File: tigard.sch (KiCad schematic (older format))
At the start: 84 parts, among them J1 USB_C_Receptacle_USB2.0, J2 JTAG, J3 UART, J4 SPI, J5 SWD, J6 I2C, Q1 BSH103, SW1 SW_DP4T, SW2 SW_DPDT, U1 AP7365-18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

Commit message: Layout routing complete, RHL fixes, xtal caps
* Finish first round of routing (needs to be reviewed, reworked in some
  places probably)
* Fix the RHL footprint (paste shouldn't be copper layers, thermal pad
  should be a polygon)
* Add 30pF capacitors to the xtal (based off estimated Cstray of 5pF)
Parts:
- added C23, C24: 30pF, Capacitor_SMD:C_0402_1005Metric, symbol Device:C_Small
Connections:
- net GND: now also C23.2, C24.2
- net USB_DN: now also J1.A7 (D-), J1.B7 (D-)
- net USB_DP: now also J1.A6 (D+), J1.B6 (D+)
- net at U3.2 (OSCI), Y1.1: now also C23.1
- net at U3.3 (OSCO), Y1.3: now also C24.1
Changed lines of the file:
@@
 NoConn ~ 1900 2100
 NoConn ~ 1900 2200
-Text Label 2600 1700 2    50   ~ 0
+Text Label 2250 1800 2    50   ~ 0
 USB_DP
-Text Label 2600 1600 2    50   ~ 0
+Text Label 2250 1600 2    50   ~ 0
 USB_DN
 $Comp
@@
 U 1 1 5EE8326F
 P 1100 7850
-F 0 "Y1" V 1054 7607 50  0000 R CNN
-F 1 "12MHz" V 1145 7607 50  0000 R CNN
+F 0 "Y1" V 1050 7550 50  0000 L CNN
+F 1 "12MHz" V 1150 7450 50  0000 L CNN
 F 2 "Crystal:Crystal_SMD_3225-4Pin_3.2x2.5mm" H 1100 7850 50  0001 C CNN
 F 3 "~" H 1100 7850 50  0001 C CNN
@@
 $EndComp
 Wire Wire Line
-	900  7850 900  8250
-Wire Wire Line
-	900  8250 1400 8250
-Wire Wire Line
 	1400 8300 1400 8250
-Connection ~ 1400 8250
-Wire Wire Line
-	1400 8250 1500 8250
 $Comp
 L power:GND #PWR0129
@@
 	1    0    0    -1
 $EndComp
+$Comp
+L Device:C_Small C23
+U 1 1 5EE9988B
+P 850 7650
+F 0 "C23" V 621 7650 50  0000 C CNN
+F 1 "30pF" V 712 7650 50  0000 C CNN
+F 2 "Capacitor_SMD:C_0402_1005Metric" H 850 7650 50  0001 C CNN
+F 3 "~" H 850 7650 50  0001 C CNN
+F 4 "CL05C300JB5NNNC" V 850 7650 50  0001 C CNN "P/N"
+F 5 "C159804" V 850 7650 50  0001 C CNN "LCSC"
+F 6 "cap-cer-0402-22pF" V 850 7650 50  0001 C CNN "Key"
+	1    850  7650
+	0    1    1    0
+$EndComp
+Wire Wire Line
+	1400 8250 1500 8250
+Wire Wire Line
+	950  7650 1100 7650
+Connection ~ 1100 7650
+Wire Wire Line
+	950  8050 1100 8050
+Connection ~ 1100 8050
+$Comp
+L power:GND #PWR01
+U 1 1 5F06B15D
+P 650 8050
+F 0 "#PWR01" H 650 7800 50  0001 C CNN
+F 1 "GND" H 655 7877 50  0000 C CNN
+F 2 "" H 650 8050 50  0001 C CNN
+F 3 "" H 650 8050 50  0001 C CNN
+	1    650  8050
+	1    0    0    -1
+$EndComp
+Wire Wire Line
+	650  8050 750  8050
+Wire Wire Line
+	900  7850 650  7850
+Wire Wire Line
+	650  7850 650  8050
+Connection ~ 650  8050
+Wire Wire Line
+	750  7650 650  7650
+Wire Wire Line
+	650  7650 650  7850
+Connection ~ 650  7850
+$Comp
+L Device:C_Small C24
+U 1 1 5F135A55
+P 850 8050
+F 0 "C24" V 987 8050 50  0000 C CNN
+F 1 "30pF" V 1078 8050 50  0000 C CNN
+F 2 "Capacitor_SMD:C_0402_1005Metric" H 850 8050 50  0001 C CNN
+F 3 "~" H 850 8050 50  0001 C CNN
+F 4 "CL05C300JB5NNNC" V 850 8050 50  0001 C CNN "P/N"
+F 5 "C159804" V 850 8050 50  0001 C CNN "LCSC"
+F 6 "cap-cer-0402-22pF" V 850 8050 50  0001 C CNN "Key"
+	1    850  8050
+	0    1    1    0
+$EndComp
+Wire Wire Line
+	1900 1800 1950 1800
+Wire Wire Line
+	2250 1600 1950 1600
+Wire Wire Line
+	1900 1700 1950 1700
+Wire Wire Line
+	1950 1700 1950 1800
+Connection ~ 1950 1800
+Wire Wire Line
+	1950 1800 2250 1800
+Wire Wire Line
+	1900 1500 1950 1500
+Wire Wire Line
+	1950 1500 1950 1600
+Connection ~ 1950 1600
+Wire Wire Line
+	1950 1600 1900 1600
 $EndSCHEMATC

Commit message: Redesign
* Designed completely in metric, no mixing units
* RoundRect pads
* Comb for resistor arrays
* VREG on inner power layer
* Switch to SMD SWD connector
* OSHW logo on front & back
* License and copyright info
* Remove reference designators
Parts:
- J5: footprint Connector_PinHeader_1.27mm:PinHeader_2x05_P1.27mm_Vertical -> Connector_PinHeader_1.27mm:PinHeader_2x05_P1.27mm_Vertical_SMD
- Q1: footprint Package_TO_SOT_SMD:SOT-23 -> tigard:SOT-23_RoundRect
- RN1, RN2, RN3, RN4, RN5, RN6, RN7, RN8: footprint Resistor_SMD:R_Array_Convex_4x0402 -> tigard:R_Array_Convex_4x0402_RoundRect
- U1, U2: footprint Package_TO_SOT_SMD:SOT-23-5 -> tigard:SOT-23-5_RoundRect
- U4: footprint Package_TO_SOT_SMD:SOT-23-6 -> tigard:SOT-23-6_RoundRect
- Y1: footprint Crystal:Crystal_SMD_3225-4Pin_3.2x2.5mm -> tigard:Crystal_SMD_3225-4Pin_3.2x2.5mm_RoundRect
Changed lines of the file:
@@
 NoConn ~ 1900 2100
 NoConn ~ 1900 2200
-Text Label 2250 1800 2    50   ~ 0
-USB_DP
-Text Label 2250 1600 2    50   ~ 0
-USB_DN
 $Comp
 L Device:R_Small R1
@@
 F 0 "U1" H 3600 1375 50  0000 C CNN
 F 1 "AP7365-18" H 3600 1284 50  0000 C CNN
-F 2 "Package_TO_SOT_SMD:SOT-23-5" H 3700 1350 50  0001 C CNN
+F 2 "tigard:SOT-23-5_RoundRect" H 3700 1350 50  0001 C CNN
 F 3 "" H 3600 1050 50  0001 C CNN
 F 4 "AP7365-18WG-7" H 3600 1450 50  0001 C CNN "P/N"
@@
 F 0 "U2" H 5100 1375 50  0000 C CNN
 F 1 "AP7365-33" H 5100 1284 50  0000 C CNN
-F 2 "Package_TO_SOT_SMD:SOT-23-5" H 5200 1350 50  0001 C CNN
+F 2 "tigard:SOT-23-5_RoundRect" H 5200 1350 50  0001 C CNN
 F 3 "" H 5100 1050 50  0001 C CNN
 F 4 "AP7365-33WG-7" H 5100 1450 50  0001 C CNN "P/N"
@@
 F 0 "Q1" H 7655 1946 50  0000 L CNN
 F 1 "BSH103" H 7655 1855 50  0000 L CNN
-F 2 "Package_TO_SOT_SMD:SOT-23" H 7650 2000 50  0001 C CNN
+F 2 "tigard:SOT-23_RoundRect" H 7650 2000 50  0001 C CNN
 F 3 "~" H 7450 1900 50  0001 C CNN
 F 4 "BSH103,235" H 7450 1900 50  0001 C CNN "P/N"
@@
 F 0 "J5" H 10400 2817 50  0000 C CNN
 F 1 "SWD" H 10400 2726 50  0000 C CNN
-F 2 "Connector_PinHeader_1.27mm:PinHeader_2x05_P1.27mm_Vertical" H 10350 2400 50  0001 C CNN
+F 2 "Connector_PinHeader_1.27mm:PinHeader_2x05_P1.27mm_Vertical_SMD" H 10350 2400 50  0001 C CNN
 F 3 "~" H 10350 2400 50  0001 C CNN
 F 4 "20021111-00010T4LF" H 10350 2400 50  0001 C CNN "P/N"
@@
 $EndComp
 NoConn ~ 10150 2500
-NoConn ~ 10650 2500
-NoConn ~ 10650 2400
 Text Label 9800 2200 0    50   ~ 0
 VTARGET
 Text Label 10900 2200 2    50   ~ 0
 SWDIO
-Text Label 10900 2300 2    50   ~ 0
-TCK
 Text Label 10900 2600 2    50   ~ 0
 ~SRST
 Wire Wire Line
 	10900 2600 10650 2600
-Wire Wire Line
-	10900 2300 10650 2300
 Wire Wire Line
 	10650 2200 10900 2200
@@
 F 0 "Y1" V 1050 7550 50  0000 L CNN
 F 1 "12MHz" V 1150 7450 50  0000 L CNN
-F 2 "Crystal:Crystal_SMD_3225-4Pin_3.2x2.5mm" H 1100 7850 50  0001 C CNN
+F 2 "tigard:Crystal_SMD_3225-4Pin_3.2x2.5mm_RoundRect" H 1100 7850 50  0001 C CNN
 F 3 "~" H 1100 7850 50  0001 C CNN
 F 4 "X322512MSB4SI" V 1100 7850 50  0001 C CNN "P/N"
@@
 F 0 "U4" H 3100 9900 50  0000 C CNN
 F 1 "93LC46BT-I/OT" H 3050 9800 50  0000 C CNN
-F 2 "Package_TO_SOT_SMD:SOT-23-6" H 2700 10100 50  0001 C CNN
+F 2 "tigard:SOT-23-6_RoundRect" H 2700 10100 50  0001 C CNN
 F 3 "http://ww1.microchip.com/downloads/en/DeviceDoc/20001749K.pdf" H 2700 10100 50  0001 C CNN
 F 4 "93LC56BT-I/OT" H 2700 10100 50  0001 C CNN "P/N"
@@
 Wire Wire Line
 	5450 5100 5450 5200
-$Comp
-L Device:R_Pack04 RN1
-U 1 1 5FBD884A
-P 5250 5650
-F 0 "RN1" V 4833 5650 50  0000 C CNN
-F 1 "100k" V 4924 5650 50  0000 C CNN
-F 2 "Resistor_SMD:R_Array_Convex_4x0402" V 5525 5650 50  0001 C CNN
-F 3 "~" H 5250 5650 50  0001 C CNN
-F 4 "4D02WGJ0104TCE" V 5250 5650 50  0001 C CNN "P/N"
-F 5 "C25724" V 5250 5650 50  0001 C CNN "LCSC"
-F 6 "res-0402cv-array-4-100k" V 5250 5650 50  0001 C CNN "Key"
-	1    5250 5650
-	0    1    1    0
-$EndComp
 Wire Wire Line
 	5050 6150 5000 6150
@@
 Wire Wire Line
 	7100 7150 7500 7150
-$Comp
-L Device:R_Pack04 RN5
-U 1 1 601ADA09
-P 5550 7500
-F 0 "RN5" V 5133 7500 50  0000 C CNN
-F 1 "100" V 5224 7500 50  0000 C CNN
-F 2 "Resistor_SMD:R_Array_Convex_4x0402" V 5825 7500 50  0001 C CNN
-F 3 "~" H 5550 7500 50  0001 C CNN
-F 4 "4D02WGJ0101TCE" V 5550 7500 50  0001 C CNN "P/N"
-F 5 "C48442" V 5550 7500 50  0001 C CNN "LCSC"
-F 6 "res-0402cv-array-4-100" V 5550 7500 50  0001 C CNN "Key"
-	1    5550 7500
-	0    1    1    0
-$EndComp
 Wire Wire Line
 	5350 8000 5300 8000
@@
 	7050 4400 7450 4400
 $Comp
-L Device:R_Pack04 RN6
-U 1 1 611E05C2
-P 5550 7900
-F 0 "RN6" V 5783 7900 50  0000 C CNN
-F 1 "100" V 5874 7900 50  0000 C CNN
-F 2 "Resistor_SMD:R_Array_Convex_4x0402" V 5825 7900 50  0001 C CNN
-F 3 "~" H 5550 7900 50  0001 C CNN
-F 4 "4D02WGJ0101TCE" V 5550 7900 50  0001 C CNN "P/N"
-F 5 "C48442" V 5550 7900 50  0001 C CNN "LCSC"
-F 6 "res-0402cv-array-4-100" V 5550 7900 50  0001 C CNN "Key"
-	1    5550 7900
-	0    1    1    0
-$EndComp
-$Comp
 L Device:R_Pack04 RN3
 U 1 1 6123B61B
@@
 F 0 "RN3" V 7033 5650 50  0000 C CNN
 F 1 "100" V 7124 5650 50  0000 C CNN
-F 2 "Resistor_SMD:R_Array_Convex_4x0402" V 7725 5650 50  0001 C CNN
+F 2 "tigard:R_Array_Convex_4x0402_RoundRect" V 7725 5650 50  0001 C CNN
 F 3 "~" H 7450 5650 50  0001 C CNN
 F 4 "4D02WGJ0101TCE" V 7450 5650 50  0001 C CNN "P/N"
@@
 $EndComp
 $Comp
-L Device:R_Pack04 RN4
-U 1 1 6123C1F3
-P 7450 6050
-F 0 "RN4" V 7683 6050 50  0000 C CNN
-F 1 "100" V 7774 6050 50  0000 C CNN
-F 2 "Resistor_SMD:R_Array_Convex_4x0402" V 7725 6050 50  0001 C CNN
-F 3 "~" H 7450 6050 50  0001 C CNN
-F 4 "4D02WGJ0101TCE" V 7450 6050 50  0001 C CNN "P/N"
-F 5 "C48442" V 7450 6050 50  0001 C CNN "LCSC"
-F 6 "res-0402cv-array-4-100" V 7450 6050 50  0001 C CNN "Key"
-	1    7450 6050
-	0    1    1    0
-$EndComp
-$Comp
-L Device:R_Pack04 RN2
-U 1 1 612C4752
-P 5250 6050
-F 0 "RN2" V 5483 6050 50  0000 C CNN
-F 1 "100k" V 5574 6050 50  0000 C CNN
-F 2 "Resistor_SMD:R_Array_Convex_4x0402" V 5525 6050 50  0001 C CNN
-F 3 "~" H 5250 6050 50  0001 C CNN
-F 4 "4D02WGJ0104TCE" V 5250 6050 50  0001 C CNN "P/N"
-F 5 "C25724" V 5250 6050 50  0001 C CNN "LCSC"
-F 6 "res-0402cv-array-4-100k" V 5250 6050 50  0001 C CNN "Key"
-	1    5250 6050
-	0    1    1    0
-$EndComp
-$Comp
 L Device:R_Pack04 RN7
 U 1 1 612C4DF4
@@
 F 0 "RN7" V 7333 7500 50  0000 C CNN
 F 1 "100k" V 7424 7500 50  0000 C CNN
-F 2 "Resistor_SMD:R_Array_Convex_4x0402" V 8025 7500 50  0001 C CNN
+F 2 "tigard:R_Array_Convex_4x0402_RoundRect" V 8025 7500 50  0001 C CNN
 F 3 "~" H 7750 7500 50  0001 C CNN
 F 4 "4D02WGJ0104TCE" V 7750 7500 50  0001 C CNN "P/N"
@@
 F 6 "res-0402cv-array-4-100k" V 7750 7500 50  0001 C CNN "Key"
 	1    7750 7500
-	0    1    1    0
-$EndComp
-$Comp
-L Device:R_Pack04 RN8
-U 1 1 612C5897
-P 7750 7900
-F 0 "RN8" V 7983 7900 50  0000 C CNN
-F 1 "100k" V 8074 7900 50  0000 C CNN
-F 2 "Resistor_SMD:R_Array_Convex_4x0402" V 8025 7900 50  0001 C CNN
-F 3 "~" H 7750 7900 50  0001 C CNN
-F 4 "4D02WGJ0104TCE" V 7750 7900 50  0001 C CNN "P/N"
-F 5 "C25724" V 7750 7900 50  0001 C CNN "LCSC"
-F 6 "res-0402cv-array-4-100k" V 7750 7900 50  0001 C CNN "Key"
-	1    7750 7900
 	0    1    1    0
 $EndComp
@@
 $EndComp
 Wire Wire Line
+	1900 1500 1950 1500
+Wire Wire Line
+	1950 1600 1900 1600
+Wire Wire Line
+	1950 1500 1950 1600
+Wire Wire Line
 	1900 1800 1950 1800
 Wire Wire Line
-	2250 1600 1950 1600
+	1950 1700 1950 1800
 Wire Wire Line
 	1900 1700 1950 1700
-Wire Wire Line
-	1950 1700 1950 1800
+Text Label 2650 1800 2    50   ~ 0
+USB_DP
+Text Label 2650 1600 2    50   ~ 0
+USB_DN
+Wire Wire Line
+	1950 1600 2650 1600
+Connection ~ 1950 1600
+Wire Wire Line
+	1950 1800 2650 1800
 Connection ~ 1950 1800
-Wire Wire Line
-	1950 1800 2250 1800
-Wire Wire Line
-	1900 1500 1950 1500
-Wire Wire Line
-	1950 1500 1950 1600
-Connection ~ 1950 1600
-Wire Wire Line
-	1950 1600 1900 1600
+NoConn ~ 10650 2400
+NoConn ~ 10650 2500
+Text Label 10900 2300 2    50   ~ 0
+TCK
+Wire Wire Line
+	10900 2300 10650 2300
+$Comp
+L Device:R_Pack04 RN4
+U 1 1 5ED37960
+P 7450 6050
+F 0 "RN4" V 7683 6050 50  0000 C CNN
+F 1 "100" V 7774 6050 50  0000 C CNN
+F 2 "tigard:R_Array_Convex_4x0402_RoundRect" V 7725 6050 50  0001 C CNN
+F 3 "~" H 7450 6050 50  0001 C CNN
+F 4 "4D02WGJ0101TCE" V 7450 6050 50  0001 C CNN "P/N"
+F 5 "C48442" V 7450 6050 50  0001 C CNN "LCSC"
+F 6 "res-0402cv-array-4-100" V 7450 6050 50  0001 C CNN "Key"
+	1    7450 6050
+	0    1    1    0
+$EndComp
+$Comp
+L Device:R_Pack04 RN5
+U 1 1 5ED9A0E0
+P 5550 7500
+F 0 "RN5" V 5133 7500 50  0000 C CNN
+F 1 "100" V 5224 7500 50  0000 C CNN
+F 2 "tigard:R_Array_Convex_4x0402_RoundRect" V 5825 7500 50  0001 C CNN
+F 3 "~" H 5550 7500 50  0001 C CNN
+F 4 "4D02WGJ0101TCE" V 5550 7500 50  0001 C CNN "P/N"
+F 5 "C48442" V 5550 7500 50  0001 C CNN "LCSC"
+F 6 "res-0402cv-array-4-100" V 5550 7500 50  0001 C CNN "Key"
+	1    5550 7500
+	0    1    1    0
+$EndComp
+$Comp
+L Device:R_Pack04 RN6
+U 1 1 5ED9AF75
+P 5550 7900
+F 0 "RN6" V 5783 7900 50  0000 C CNN
+F 1 "100" V 5874 7900 50  0000 C CNN
+F 2 "tigard:R_Array_Convex_4x0402_RoundRect" V 5825 7900 50  0001 C CNN
+F 3 "~" H 5550 7900 50  0001 C CNN
+F 4 "4D02WGJ0101TCE" V 5550 7900 50  0001 C CNN "P/N"
+F 5 "C48442" V 5550 7900 50  0001 C CNN "LCSC"
+F 6 "res-0402cv-array-4-100" V 5550 7900 50  0001 C CNN "Key"
+	1    5550 7900
+	0    1    1    0
+$EndComp
+$Comp
+L Device:R_Pack04 RN8
+U 1 1 5EDCD172
+P 7750 7900
+F 0 "RN8" V 7983 7900 50  0000 C CNN
+F 1 "100k" V 8074 7900 50  0000 C CNN
+F 2 "tigard:R_Array_Convex_4x0402_RoundRect" V 8025 7900 50  0001 C CNN
+F 3 "~" H 7750 7900 50  0001 C CNN
+F 4 "4D02WGJ0104TCE" V 7750 7900 50  0001 C CNN "P/N"
+F 5 "C25724" V 7750 7900 50  0001 C CNN "LCSC"
+F 6 "res-0402cv-array-4-100k" V 7750 7900 50  0001 C CNN "Key"
+	1    7750 7900
+	0    1    1    0
+$EndComp
+$Comp
+L Device:R_Pack04 RN1
+U 1 1 5EE2F88A
+P 5250 5650
+F 0 "RN1" V 4833 5650 50  0000 C CNN
+F 1 "100k" V 4924 5650 50  0000 C CNN
+F 2 "tigard:R_Array_Convex_4x0402_RoundRect" V 5525 5650 50  0001 C CNN
+F 3 "~" H 5250 5650 50  0001 C CNN
+F 4 "4D02WGJ0104TCE" V 5250 5650 50  0001 C CNN "P/N"
+F 5 "C25724" V 5250 5650 50  0001 C CNN "LCSC"
+F 6 "res-0402cv-array-4-100k" V 5250 5650 50  0001 C CNN "Key"
+	1    5250 5650
+	0    1    1    0
+$EndComp
+$Comp
+L Device:R_Pack04 RN2
+U 1 1 5EE3079F
+P 5250 6050
+F 0 "RN2" V 5483 6050 50  0000 C CNN
+F 1 "100k" V 5574 6050 50  0000 C CNN
+F 2 "tigard:R_Array_Convex_4x0402_RoundRect" V 5525 6050 50  0001 C CNN
+F 3 "~" H 5250 6050 50  0001 C CNN
+F 4 "4D02WGJ0104TCE" V 5250 6050 50  0001 C CNN "P/N"
+F 5 "C25724" V 5250 6050 50  0001 C CNN "LCSC"
+F 6 "res-0402cv-array-4-100k" V 5250 6050 50  0001 C CNN "Key"
+	1    5250 6050
+	0    1    1    0
+$EndComp
 $EndSCHEMATC

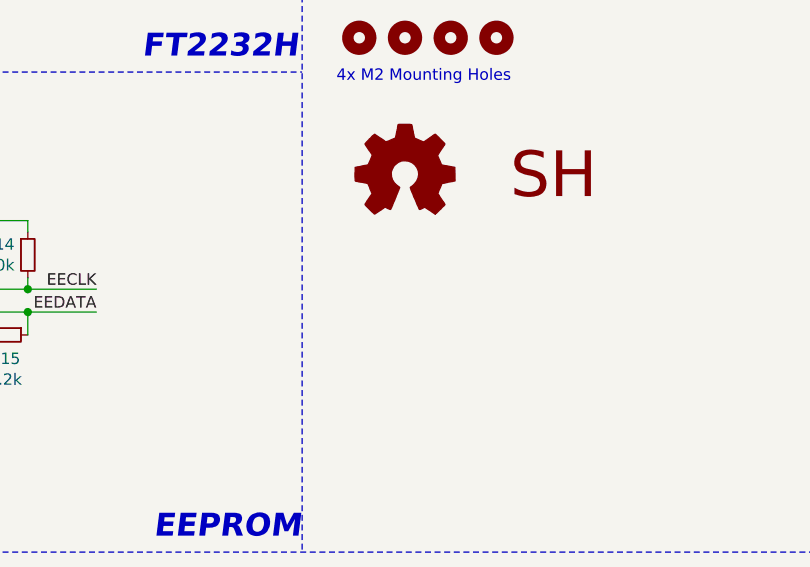
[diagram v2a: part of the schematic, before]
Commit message: Move vias out from underneath FT2232H
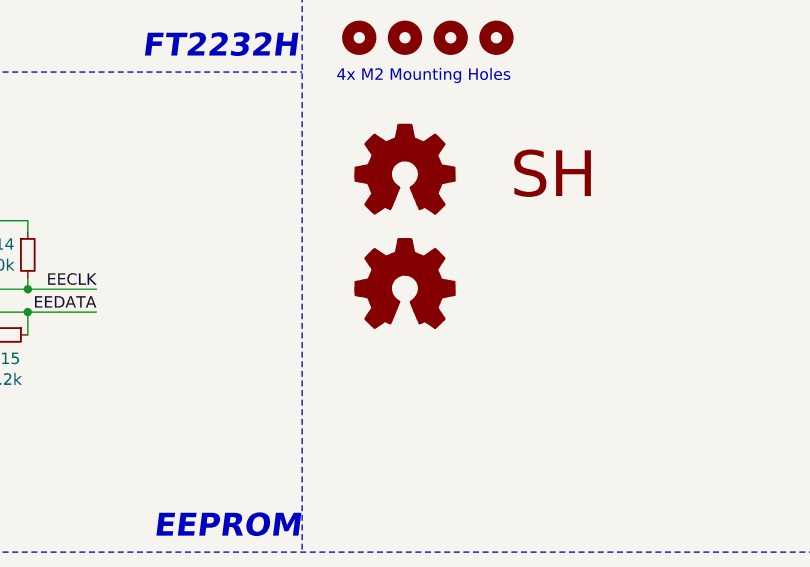
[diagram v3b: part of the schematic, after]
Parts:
- added LOGO3: Logo_Open_Hardware_Small, Symbol:OSHW-Symbol_6.7x6mm_SilkScreen, symbol Graphic:Logo_Open_Hardware_Small
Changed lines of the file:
@@
 	0    1    1    0
 $EndComp
+$Comp
+L Graphic:Logo_Open_Hardware_Small LOGO3
+U 1 1 5ED57CD6
+P 5250 10000
+F 0 "LOGO3" H 5250 10275 50  0001 C CNN
+F 1 "Logo_Open_Hardware_Small" H 5250 9775 50  0001 C CNN
+F 2 "Symbol:OSHW-Symbol_6.7x6mm_SilkScreen" H 5250 10000 50  0001 C CNN
+F 3 "~" H 5250 10000 50  0001 C CNN
+	1    5250 10000
+	1    0    0    -1
+$EndComp
 $EndSCHEMATC
